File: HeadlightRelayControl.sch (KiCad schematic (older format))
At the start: 31 parts, among them P1 CONN_01X03, P2 CONN_01X02, P3 CONN_01X02, P4 CONN_2, Q1 2N3904, Q2 2N3904

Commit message: bugfix: a 1/4 watt resistor was seeing 500mW.  broke it up into four 1/4w resistors.  this is release v2.
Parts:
- added R10, R11, R12, R13, R14, R9: 100, symbol R_0W25
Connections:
- wire segments 72 -> 80
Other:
- moved on the sheet: C1, C2, D4, D5, D6, D7, D8, D9, P2, P3, Q1, Q2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

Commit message: removing extraneous transistors. updated board labelling.
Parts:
- removed Q1, Q2: 2N3904, symbol 2N3904
- removed R1, R3: 1k, symbol R_0W25
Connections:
- wire segments 80 -> 74
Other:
- moved on the sheet: C1, C2, D4, D5, P2, P3, R10, R11, R12, R13, R14, R2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

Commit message: Added corner mounting holes.
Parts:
- added H10, H4, H8, H9: HOLE, ~, symbol HOLE
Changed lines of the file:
@@
 EESchema Schematic File Version 2
+LIBS:vref_PL
+LIBS:analog_ICs_PL
+LIBS:capacitors_PL
+LIBS:connectors_PL
+LIBS:diodes_PL
+LIBS:displays_PL
+LIBS:inductors_PL
+LIBS:LEDs_PL
+LIBS:microcontrollers_PL
+LIBS:mounting_holes_PL
+LIBS:noname-cache
+LIBS:opamps
+LIBS:opamps_PL
+LIBS:opto_PL
+LIBS:references_PL
+LIBS:regulators_PL
+LIBS:relays_PL
+LIBS:resistors_PL
+LIBS:switches_PL
+LIBS:transistors_PL
 LIBS:power
 LIBS:device
@@
 L HOLE H2
 U 1 1 550A7E8B
-P 9550 7200
-F 0 "H2" H 9550 7255 30  0000 C CNN
-F 1 "HOLE" H 9550 7140 30  0000 C CNN
-F 2 "~" H 9550 7200 60  0000 C CNN
-F 3 "~" H 9550 7200 60  0000 C CNN
-	1    9550 7200
+P 8200 7200
+F 0 "H2" H 8200 7255 30  0000 C CNN
+F 1 "HOLE" H 8200 7140 30  0000 C CNN
+F 2 "~" H 8200 7200 60  0000 C CNN
+F 3 "~" H 8200 7200 60  0000 C CNN
+	1    8200 7200
 	1    0    0    -1
 $EndComp
@@
 L HOLE H1
 U 1 1 550A7EA4
-P 9550 6950
-F 0 "H1" H 9550 7005 30  0000 C CNN
-F 1 "HOLE" H 9550 6890 30  0000 C CNN
-F 2 "~" H 9550 6950 60  0000 C CNN
-F 3 "~" H 9550 6950 60  0000 C CNN
-	1    9550 6950
+P 8200 6950
+F 0 "H1" H 8200 7005 30  0000 C CNN
+F 1 "HOLE" H 8200 6890 30  0000 C CNN
+F 2 "~" H 8200 6950 60  0000 C CNN
+F 3 "~" H 8200 6950 60  0000 C CNN
+	1    8200 6950
 	1    0    0    -1
 $EndComp
@@
 L HOLE H3
 U 1 1 550A7EAA
-P 9750 6950
-F 0 "H3" H 9750 7005 30  0000 C CNN
-F 1 "HOLE" H 9750 6890 30  0000 C CNN
-F 2 "~" H 9750 6950 60  0000 C CNN
-F 3 "~" H 9750 6950 60  0000 C CNN
-	1    9750 6950
+P 8400 6950
+F 0 "H3" H 8400 7005 30  0000 C CNN
+F 1 "HOLE" H 8400 6890 30  0000 C CNN
+F 2 "~" H 8400 6950 60  0000 C CNN
+F 3 "~" H 8400 6950 60  0000 C CNN
+	1    8400 6950
 	1    0    0    -1
 $EndComp
@@
 L FEET H5
 U 1 1 550B95E3
-P 10150 6950
-F 0 "H5" H 10150 7005 30  0000 C CNN
-F 1 "FEET" H 10150 6890 30  0000 C CNN
-F 2 "~" H 10150 6950 60  0000 C CNN
-F 3 "~" H 10150 6950 60  0000 C CNN
-	1    10150 6950
+P 8800 6950
+F 0 "H5" H 8800 7005 30  0000 C CNN
+F 1 "FEET" H 8800 6890 30  0000 C CNN
+F 2 "~" H 8800 6950 60  0000 C CNN
+F 3 "~" H 8800 6950 60  0000 C CNN
+	1    8800 6950
 	1    0    0    -1
 $EndComp
@@
 L FEET H7
 U 1 1 550B95F2
-P 10350 6950
-F 0 "H7" H 10350 7005 30  0000 C CNN
-F 1 "FEET" H 10350 6890 30  0000 C CNN
-F 2 "~" H 10350 6950 60  0000 C CNN
-F 3 "~" H 10350 6950 60  0000 C CNN
-	1    10350 6950
+P 9000 6950
+F 0 "H7" H 9000 7005 30  0000 C CNN
+F 1 "FEET" H 9000 6890 30  0000 C CNN
+F 2 "~" H 9000 6950 60  0000 C CNN
+F 3 "~" H 9000 6950 60  0000 C CNN
+	1    9000 6950
 	1    0    0    -1
 $EndComp
@@
 L FEET H6
 U 1 1 550B9601
-P 10150 7200
-F 0 "H6" H 10150 7255 30  0000 C CNN
-F 1 "FEET" H 10150 7140 30  0000 C CNN
-F 2 "~" H 10150 7200 60  0000 C CNN
-F 3 "~" H 10150 7200 60  0000 C CNN
-	1    10150 7200
+P 8800 7200
+F 0 "H6" H 8800 7255 30  0000 C CNN
+F 1 "FEET" H 8800 7140 30  0000 C CNN
+F 2 "~" H 8800 7200 60  0000 C CNN
+F 3 "~" H 8800 7200 60  0000 C CNN
+	1    8800 7200
 	1    0    0    -1
 $EndComp
@@
 Wire Wire Line
 	7100 5450 7100 5600
+$Comp
+L HOLE H4
+U 1 1 550E4BBE
+P 9550 6950
+F 0 "H4" H 9550 7005 30  0000 C CNN
+F 1 "HOLE" H 9550 6890 30  0000 C CNN
+F 2 "~" H 9550 6950 60  0000 C CNN
+F 3 "~" H 9550 6950 60  0000 C CNN
+	1    9550 6950
+	1    0    0    -1
+$EndComp
+$Comp
+L HOLE H8
+U 1 1 550E4BCD
+P 9550 7200
+F 0 "H8" H 9550 7255 30  0000 C CNN
+F 1 "HOLE" H 9550 7140 30  0000 C CNN
+F 2 "~" H 9550 7200 60  0000 C CNN
+F 3 "~" H 9550 7200 60  0000 C CNN
+	1    9550 7200
+	1    0    0    -1
+$EndComp
+$Comp
+L HOLE H9
+U 1 1 550E4BDC
+P 9800 6950
+F 0 "H9" H 9800 7005 30  0000 C CNN
+F 1 "HOLE" H 9800 6890 30  0000 C CNN
+F 2 "~" H 9800 6950 60  0000 C CNN
+F 3 "~" H 9800 6950 60  0000 C CNN
+	1    9800 6950
+	1    0    0    -1
+$EndComp
+$Comp
+L HOLE H10
+U 1 1 550E4BEB
+P 9800 7200
+F 0 "H10" H 9800 7255 30  0000 C CNN
+F 1 "HOLE" H 9800 7140 30  0000 C CNN
+F 2 "~" H 9800 7200 60  0000 C CNN
+F 3 "~" H 9800 7200 60  0000 C CNN
+	1    9800 7200
+	1    0    0    -1
+$EndComp
 $EndSCHEMATC

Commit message: creating PDF of schematic
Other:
- note added: "Jumper keeps low beams\non when high beams engaged."
- moved on the sheet: C1, C2, D4, D5, D6, D7, D8, D9, P2, P3, R10, R11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

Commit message: adding v3 board design with constant current sinks on relay coils.
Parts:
- removed D4, D5: 1N4001, symbol DIODE
- removed P2: CONN_01X02, symbol CONN_01X02
- removed R13, R14, R2, R4: 100, symbol R_0W25
- added D8, D9: 1N4001, symbol DIODE
- added P4: CONN_01X02, symbol CONN_01X02
- added Q1, Q2, Q3, Q4, Q5, Q6: 2N3904, ~, symbol 2N3904
- added R5: 10k, symbol R_0W25
- added R6, R7, R8: 10, symbol R_0W25
- C1, C2: value 100uF -> 220uF
- R10, R11, R12: value 100 -> 10
- R9: value 100 -> 10k
- renumbered D6 to D1, D7 to D2, D1 to D3, D2 to D4, D3 to D5, D8 to D6, D9 to D7, H5 to H4, H6 to H5, H7 to H6, H4 to H7, P4 to P2, R5 to R1, R6 to R2, R7 to R3, R8 to R4
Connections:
- wire segments 74 -> 94
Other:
- note added: "HOLD current (CC 65mA)"
- note added: "PICK\ncurrent"
- moved on the sheet: D3, D4, D5, D6, D7, P1, P2, R3, R4

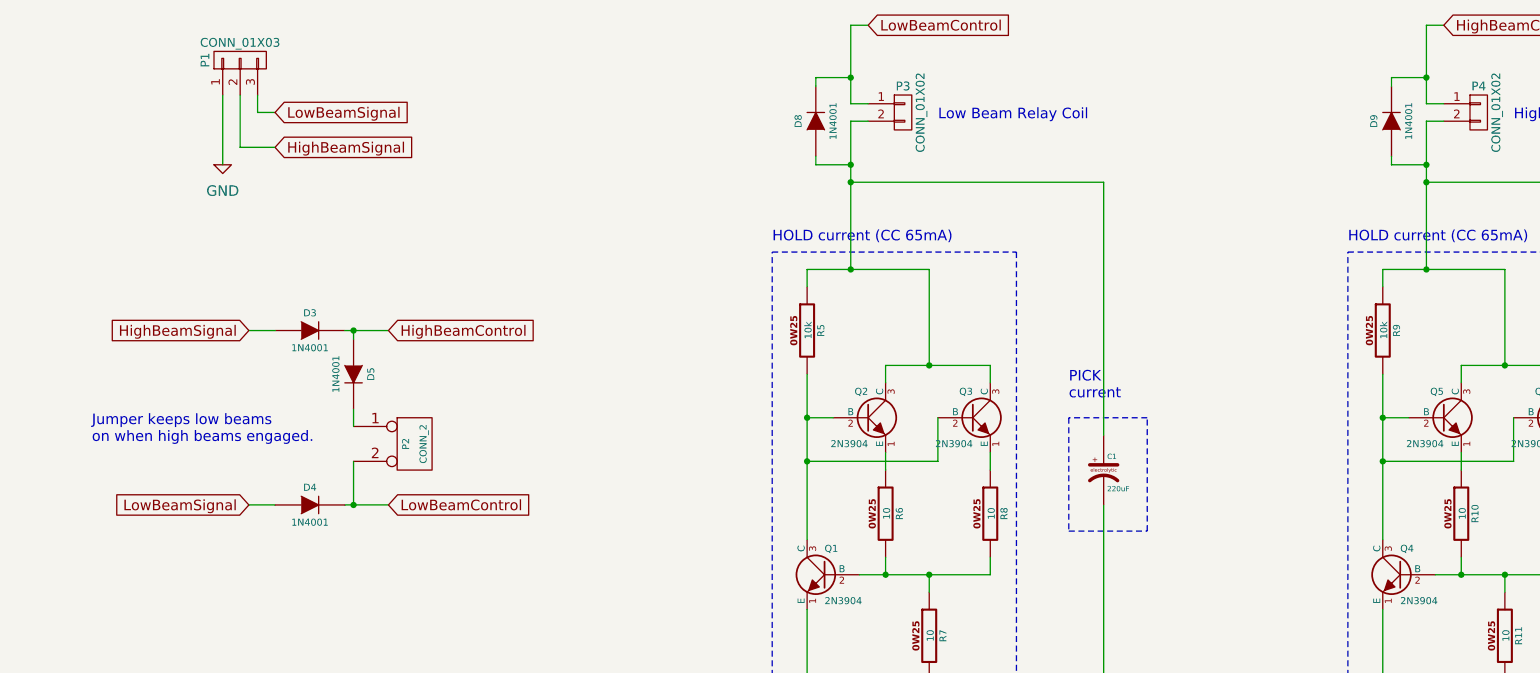
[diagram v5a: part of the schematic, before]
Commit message: changing 1N4001 diodes to schottky 1N5817. updating diode footprints. adding substitution notes to schematic.
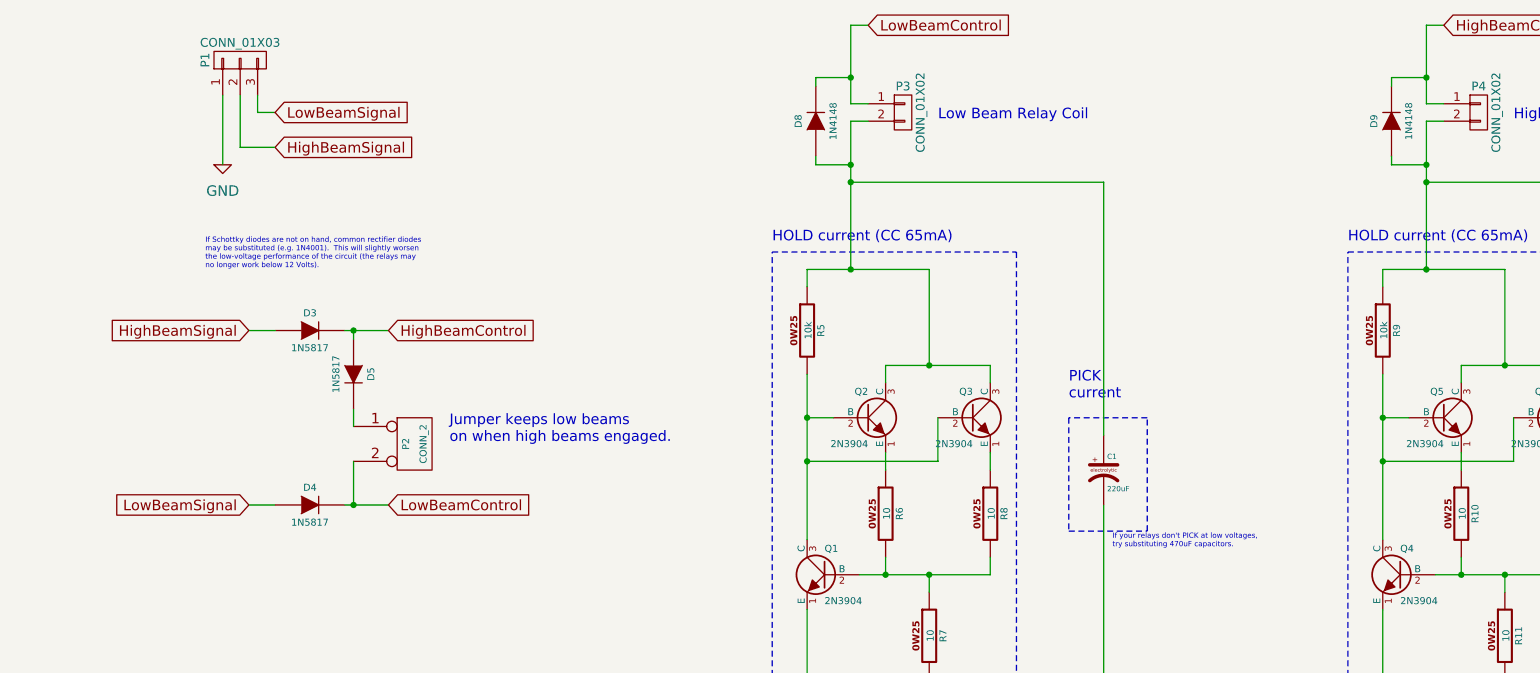
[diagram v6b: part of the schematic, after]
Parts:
- D3, D4, D5: value 1N4001 -> 1N5817
- D8, D9: value 1N4001 -> 1N4148
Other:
- note added: "If Schottky diodes are not on hand, common rectifier diodes\nmay be substituted (e.g. 1N4001). This will slightly worsen\nthe low-voltage performance of the circuit (the relays may\nno longer work below 12 Volts)."
- note added: "If your relays don't PICK at low voltages,\ntry substituting 470uF capacitors."
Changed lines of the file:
@@
 LIBS:capacitors_PL
 LIBS:connectors_PL
-LIBS:diodes_PL
+LIBS:PL_diodes
 LIBS:displays_PL
 LIBS:inductors_PL
@@
 Sheet 1 1
 Title ""
-Date "24 mar 2015"
+Date "2 apr 2015"
 Rev ""
 Comp ""
@@
 P 2100 2850
 F 0 "D3" H 2100 2950 40  0000 C CNN
-F 1 "1N4001" H 2100 2750 40  0000 C CNN
+F 1 "1N5817" H 2100 2750 40  0000 C CNN
 F 2 "" H 2100 2850 60  0000 C CNN
 F 3 "" H 2100 2850 60  0000 C CNN
@@
 P 2100 3850
 F 0 "D4" H 2100 3950 40  0000 C CNN
-F 1 "1N4001" H 2100 3750 40  0000 C CNN
+F 1 "1N5817" H 2100 3750 40  0000 C CNN
 F 2 "" H 2100 3850 60  0000 C CNN
 F 3 "" H 2100 3850 60  0000 C CNN
@@
 P 2350 3100
 F 0 "D5" H 2350 3200 40  0000 C CNN
-F 1 "1N4001" H 2350 3000 40  0000 C CNN
+F 1 "1N5817" H 2350 3000 40  0000 C CNN
 F 2 "" H 2350 3100 60  0000 C CNN
 F 3 "" H 2350 3100 60  0000 C CNN
@@
 	1    0    0    -1
 $EndComp
-Text Notes 850  3500 0    60   ~ 0
+Text Notes 2900 3500 0    60   ~ 0
 Jumper keeps low beams\non when high beams engaged.
 $Comp
@@
 P 5000 1650
 F 0 "D8" H 5000 1750 40  0000 C CNN
-F 1 "1N4001" H 5000 1550 40  0000 C CNN
+F 1 "1N4148" H 5000 1550 40  0000 C CNN
 F 2 "" H 5000 1650 60  0000 C CNN
 F 3 "" H 5000 1650 60  0000 C CNN
@@
 P 8300 1650
 F 0 "D9" H 8300 1750 40  0000 C CNN
-F 1 "1N4001" H 8300 1550 40  0000 C CNN
+F 1 "1N4148" H 8300 1550 40  0000 C CNN
 F 2 "" H 8300 1650 60  0000 C CNN
 F 3 "" H 8300 1650 60  0000 C CNN
@@
 Connection ~ 5350 4950
 Connection ~ 8650 4950
+Text Notes 1500 2500 0    30   ~ 0
+If Schottky diodes are not on hand, common rectifier diodes\nmay be substituted (e.g. 1N4001).  This will slightly worsen\nthe low-voltage performance of the circuit (the relays may\nno longer work below 12 Volts).
+Text Notes 6700 4100 0    30   ~ 0
+If your relays don't PICK at low voltages,\ntry substituting 470uF capacitors.
 $EndSCHEMATC
